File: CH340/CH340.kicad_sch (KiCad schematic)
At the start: 11 parts, among them J18 USB_B_Mini, U28 CH340G, Y1 Crystal

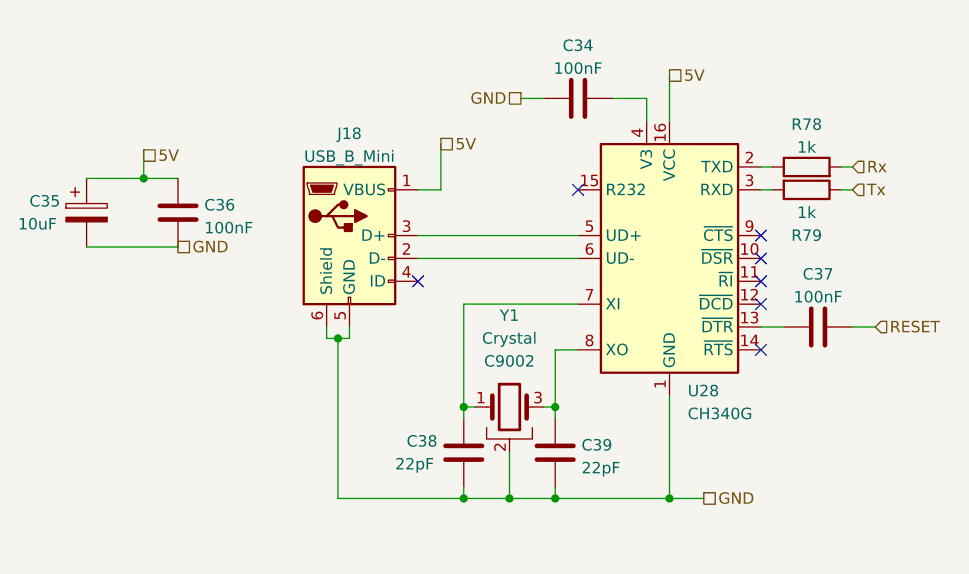
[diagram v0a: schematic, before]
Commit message: moved some schematic scheets to their own folders and routed a board with it. This allow for re-use of PCB parts.
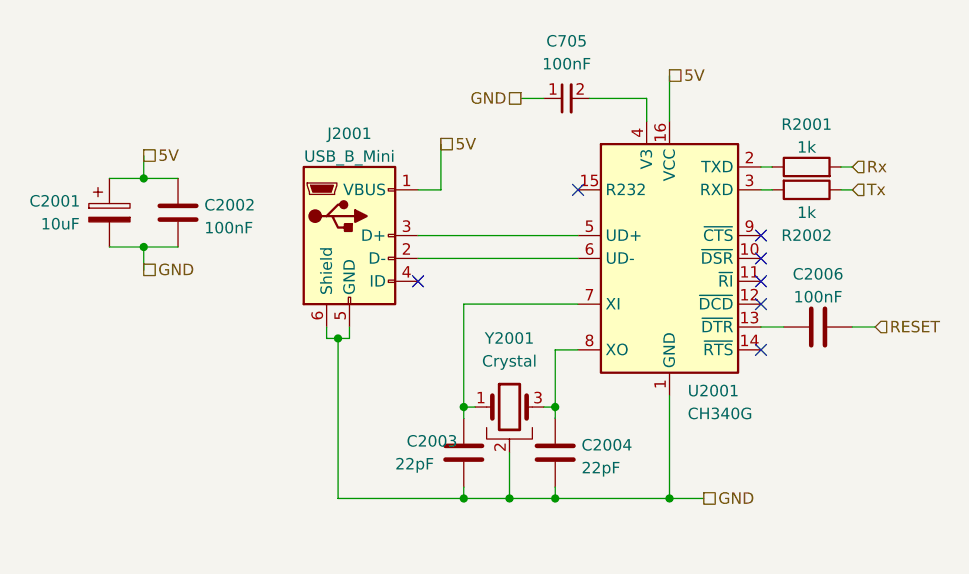
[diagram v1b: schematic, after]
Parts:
- removed C34: 100nF, Capacitor_SMD:C_0603_1608Metric_Pad1.08x0.95mm_HandSolder, symbol Device:C
- added C705: 100nF, Capacitor_SMD:C_0402_1005Metric, symbol capacitor_miscellaneous:C_0402_100nF
- C2001: renamed from C35; footprint (none) -> Capacitor_SMD:C_0603_1608Metric
- C2002: renamed from C36; footprint Capacitor_SMD:C_0603_1608Metric_Pad1.08x0.95mm_HandSolder -> Capacitor_SMD:C_0603_1608Metric
- C2003: renamed from C38; footprint Capacitor_SMD:C_0603_1608Metric_Pad1.08x0.95mm_HandSolder -> Capacitor_SMD:C_0603_1608Metric
- C2004: renamed from C39; footprint Capacitor_SMD:C_0603_1608Metric_Pad1.08x0.95mm_HandSolder -> Capacitor_SMD:C_0603_1608Metric
- C2006: renamed from C37; footprint Capacitor_SMD:C_0603_1608Metric_Pad1.08x0.95mm_HandSolder -> Capacitor_SMD:C_0603_1608Metric
- J2001: renamed from J18; footprint (none) -> Connector_USB:USB_Mini-B_Lumberg_2486_01_Horizontal
- R2001: renamed from R78; footprint Resistor_SMD:R_0603_1608Metric_Pad0.98x0.95mm_HandSolder -> Resistor_SMD:R_0603_1608Metric
- R2002: renamed from R79; footprint Resistor_SMD:R_0603_1608Metric_Pad0.98x0.95mm_HandSolder -> Resistor_SMD:R_0603_1608Metric
- renumbered U28 to U2001, Y1 to Y2001
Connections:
- net GND: now also C705.1
- net at U2001.4 (V3): now also C705.2
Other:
- moved on the sheet: C2001

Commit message: added 12V boost converter (300mA max!)
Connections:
- net 5V renamed +5V
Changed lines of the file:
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@@
   (junction (at 64.77 82.55) (diameter 0) (color 0 0 0 0)
-  )
-  (junction (at 123.19 118.11) (diameter 0) (color 0 0 0 0)
   )
   (junction (at 110.49 107.95) (diameter 0) (color 0 0 0 0)
@@
     (stroke (width 0) (type default))
   )
-  (wire (pts (xy 123.19 118.11) (xy 127 118.11))
-    (stroke (width 0) (type default))
-  )
   (wire (pts (xy 86.36 118.11) (xy 100.33 118.11))
     (stroke (width 0) (type default))
@@
     (stroke (width 0) (type default))
   )
+  (wire (pts (xy 64.77 90.17) (xy 64.77 92.71))
+    (stroke (width 0) (type default))
+  )
   (wire (pts (xy 133.35 99.06) (xy 135.89 99.06))
     (stroke (width 0) (type default))
@@
     (stroke (width 0) (type default))
   )
-  (wire (pts (xy 64.77 90.17) (xy 64.77 92.71))
-    (stroke (width 0) (type default))
-  )
   (wire (pts (xy 110.49 107.95) (xy 110.49 101.6))
     (stroke (width 0) (type default))
@@
   (wire (pts (xy 86.36 100.33) (xy 87.63 100.33))
     (stroke (width 0) (type default))
-  )
-  (hierarchical_label "GND" (shape passive) (at 106.68 73.66 180) (fields_autoplaced)
-    (effects (font (size 1.27 1.27)) (justify right))
-  )
-  (hierarchical_label "5V" (shape passive) (at 64.77 80.01 0) (fields_autoplaced)
-    (effects (font (size 1.27 1.27)) (justify left))
-  )
-  (hierarchical_label "5V" (shape passive) (at 123.19 71.12 0) (fields_autoplaced)
-    (effects (font (size 1.27 1.27)) (justify left))
-  )
-  (hierarchical_label "GND" (shape passive) (at 64.77 92.71 0) (fields_autoplaced)
-    (effects (font (size 1.27 1.27)) (justify left))
   )
   (hierarchical_label "Rx" (shape input) (at 143.51 81.28 0) (fields_autoplaced)
@@
     (effects (font (size 1.27 1.27)) (justify left))
   )
-  (hierarchical_label "GND" (shape passive) (at 127 118.11 0) (fields_autoplaced)
-    (effects (font (size 1.27 1.27)) (justify left))
-  )
-  (hierarchical_label "5V" (shape passive) (at 97.79 78.74 0) (fields_autoplaced)
-    (effects (font (size 1.27 1.27)) (justify left))
+  (symbol (lib_id "power:GND") (at 64.77 92.71 0) (unit 1)
+    (in_bom yes) (on_board yes) (dnp no) (fields_autoplaced)
+    (property "Reference" "#PWR0104" (at 64.77 99.06 0)
+      (effects (font (size 1.27 1.27)) hide)
+    )
+    (property "Value" "GND" (at 64.77 97.79 0)
+      (effects (font (size 1.27 1.27)))
+    )
+    (property "Footprint" "" (at 64.77 92.71 0)
+      (effects (font (size 1.27 1.27)) hide)
+    )
+    (property "Datasheet" "" (at 64.77 92.71 0)
+      (effects (font (size 1.27 1.27)) hide)
+    )
+    (pin "1")
+    (instances
+      (project "CH340"
+        (path "/fffcb7a4-8d9e-4797-952f-70897aee5417"
+          (reference "#PWR0104") (unit 1)
+        )
+      )
+    )
   )
   (symbol (lib_id "Device:C") (at 68.58 86.36 0) (unit 1)
@@
         (path "/fffcb7a4-8d9e-4797-952f-70897aee5417"
           (reference "C706") (unit 1)
+        )
+      )
+    )
+  )
+  (symbol (lib_id "power:GND") (at 105.41 118.11 0) (unit 1)
+    (in_bom yes) (on_board yes) (dnp no) (fields_autoplaced)
+    (property "Reference" "#PWR0103" (at 105.41 124.46 0)
+      (effects (font (size 1.27 1.27)) hide)
+    )
+    (property "Value" "GND" (at 105.41 123.19 0)
+      (effects (font (size 1.27 1.27)))
+    )
+    (property "Footprint" "" (at 105.41 118.11 0)
+      (effects (font (size 1.27 1.27)) hide)
+    )
+    (property "Datasheet" "" (at 105.41 118.11 0)
+      (effects (font (size 1.27 1.27)) hide)
+    )
+    (pin "1")
+    (instances
+      (project "CH340"
+        (path "/fffcb7a4-8d9e-4797-952f-70897aee5417"
+          (reference "#PWR0103") (unit 1)
         )
       )
@@
     )
   )
+  (symbol (lib_id "power:+5V") (at 123.19 71.12 0) (unit 1)
+    (in_bom yes) (on_board yes) (dnp no) (fields_autoplaced)
+    (property "Reference" "#PWR0101" (at 123.19 74.93 0)
+      (effects (font (size 1.27 1.27)) hide)
+    )
+    (property "Value" "+5V" (at 123.19 66.04 0)
+      (effects (font (size 1.27 1.27)))
+    )
+    (property "Footprint" "" (at 123.19 71.12 0)
+      (effects (font (size 1.27 1.27)) hide)
+    )
+    (property "Datasheet" "" (at 123.19 71.12 0)
+      (effects (font (size 1.27 1.27)) hide)
+    )
+    (pin "1")
+    (instances
+      (project "CH340"
+        (path "/fffcb7a4-8d9e-4797-952f-70897aee5417"
+          (reference "#PWR0101") (unit 1)
+        )
+      )
+    )
+  )
   (symbol (lib_id "capacitor_miscellaneous:C_0402_100nF") (at 111.76 73.66 90) (unit 1)
     (in_bom yes) (on_board yes) (dnp no) (fields_autoplaced)
@@
         (path "/fffcb7a4-8d9e-4797-952f-70897aee5417"
           (reference "C701") (unit 1)
+        )
+      )
+    )
+  )
+  (symbol (lib_id "power:+5V") (at 97.79 78.74 0) (unit 1)
+    (in_bom yes) (on_board yes) (dnp no) (fields_autoplaced)
+    (property "Reference" "#PWR0105" (at 97.79 82.55 0)
+      (effects (font (size 1.27 1.27)) hide)
+    )
+    (property "Value" "+5V" (at 97.79 73.66 0)
+      (effects (font (size 1.27 1.27)))
+    )
+    (property "Footprint" "" (at 97.79 78.74 0)
+      (effects (font (size 1.27 1.27)) hide)
+    )
+    (property "Datasheet" "" (at 97.79 78.74 0)
+      (effects (font (size 1.27 1.27)) hide)
+    )
+    (pin "1")
+    (instances
+      (project "CH340"
+        (path "/fffcb7a4-8d9e-4797-952f-70897aee5417"
+          (reference "#PWR0105") (unit 1)
         )
       )
@@
         )
       )
+    )
+  )
+  (symbol (lib_id "power:GND") (at 106.68 73.66 0) (unit 1)
+    (in_bom yes) (on_board yes) (dnp no) (fields_autoplaced)
+    (property "Reference" "#PWR0106" (at 106.68 80.01 0)
+      (effects (font (size 1.27 1.27)) hide)
+    )
+    (property "Value" "GND" (at 106.68 78.74 0)
+      (effects (font (size 1.27 1.27)))
+    )
+    (property "Footprint" "" (at 106.68 73.66 0)
+      (effects (font (size 1.27 1.27)) hide)
+    )
+    (property "Datasheet" "" (at 106.68 73.66 0)
+      (effects (font (size 1.27 1.27)) hide)
+    )
+    (pin "1")
+    (instances
+      (project "CH340"
+        (path "/fffcb7a4-8d9e-4797-952f-70897aee5417"
+          (reference "#PWR0106") (unit 1)
+        )
+      )
+    )
+  )
+  (symbol (lib_id "power:+5V") (at 64.77 80.01 0) (unit 1)
+    (in_bom yes) (on_board yes) (dnp no) (fields_autoplaced)
+    (property "Reference" "#PWR0102" (at 64.77 83.82 0)
+      (effects (font (size 1.27 1.27)) hide)
+    )
+    (property "Value" "+5V" (at 64.77 74.93 0)
+      (effects (font (size 1.27 1.27)))
+    )
+    (property "Footprint" "" (at 64.77 80.01 0)
+      (effects (font (size 1.27 1.27)) hide)
+    )
+    (property "Datasheet" "" (at 64.77 80.01 0)
+      (effects (font (size 1.27 1.27)) hide)
+    )
+    (pin "1")
+    (instances
+      (project "CH340"
+        (path "/fffcb7a4-8d9e-4797-952f-70897aee5417"
+          (reference "#PWR0102") (unit 1)
+        )
+      )
